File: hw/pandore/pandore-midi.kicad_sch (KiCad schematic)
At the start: 0 parts

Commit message: added all remaining connectors (only missing M.2 now)
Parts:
- added J10: MIDI_in, reekilib_con:samesky_SDS-50J, symbol reekilib_con:MIDI_in
- added J11: MIDI_out, reekilib_con:samesky_SDS-50J, symbol reekilib_con:MIDI_out

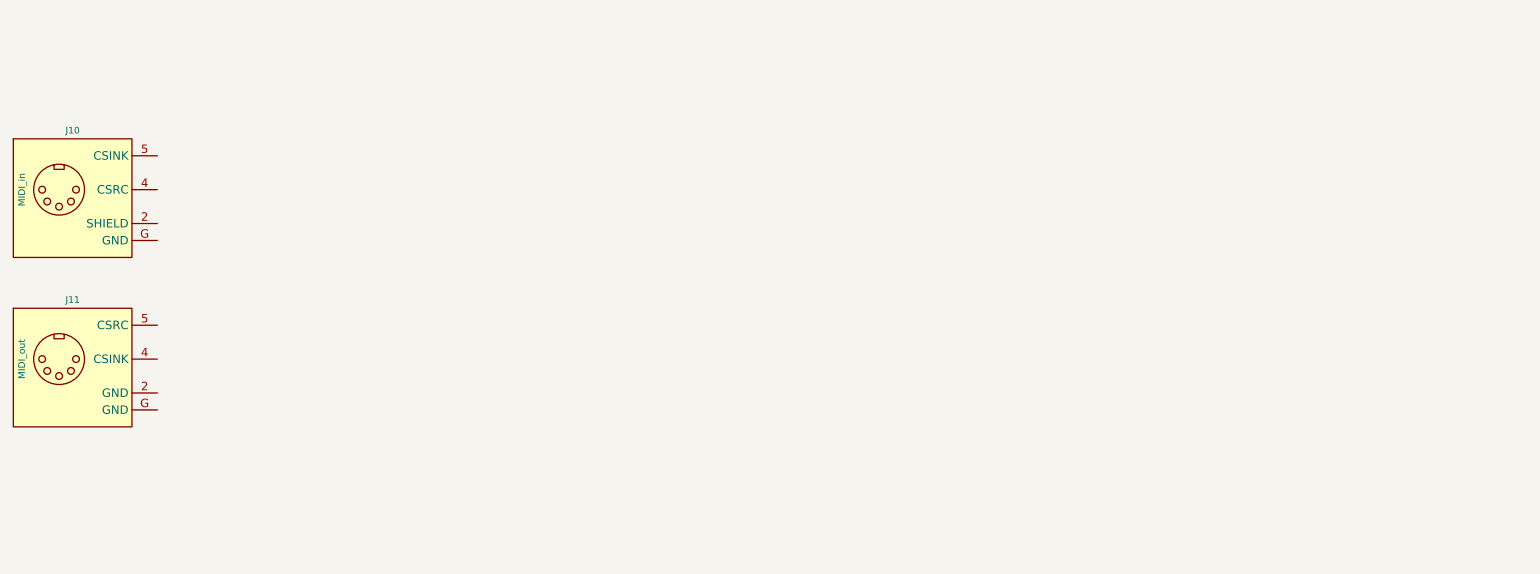
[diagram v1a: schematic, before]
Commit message: Added lots to sch and pcb: eth passive, audio codec, midi, teensy Corrected and added support for M.2
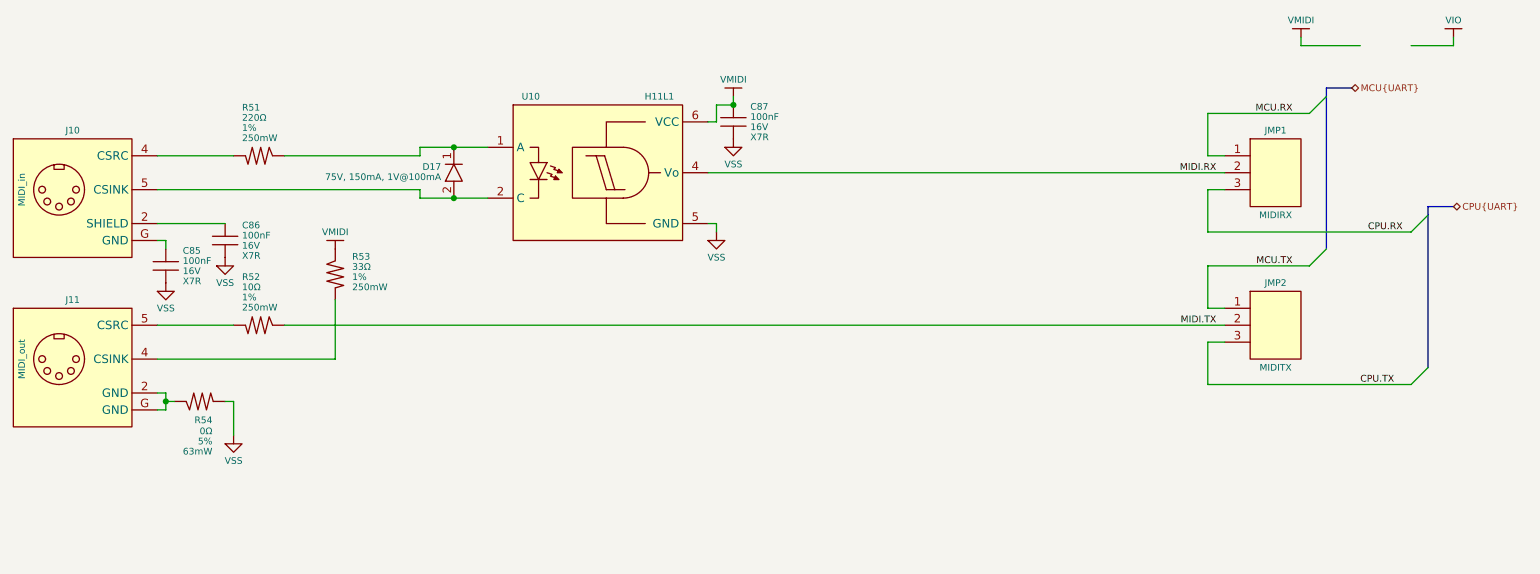
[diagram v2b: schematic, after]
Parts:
- added C85, C86, C87: ${Capacitance}, ${Voltage}, ${Dielectric}, reekilib_cap:CAPC1005, symbol reekilib_cap:cap
- added D17: ${Vr}, ${Io}, ${Vf}, reekilib_sod:sod-123, symbol reekilib_dio:diode
- added JMP1: MIDIRX, reekilib_con:HDR254P1X03-TH, symbol reekilib_con:hdr-1x3
- added JMP2: MIDITX, reekilib_con:HDR254P1X03-TH, symbol reekilib_con:hdr-1x3
- added R51, R52, R53: ${Resistance}, ${Tolerance}, ${Power}, reekilib_res:RESC2012, symbol reekilib_res:res
- added R54: ${Resistance}, ${Tolerance}, ${Power}, reekilib_res:RESC1005, symbol reekilib_res:res
- added U10: H11L1, reekilib_soic:SOIC254P1030X430-6, symbol reekilib_iso:opto_digppout
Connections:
- net at J10.2 (SHIELD): now also C86.2
- net at J10.4 (CSRC): now also R51.1
- net at J10.5 (CSINK): now also D17.2 (A), U10.2 (C)
- net at J10.G (GND): now also C85.2
- net at J11.2 (GND): now also J11.G (GND), R54.2
- net at J11.4 (CSINK): now also R53.1
- net at J11.5 (CSRC): now also R52.1
- new net: D17.1 (C), R51.2, U10.1 (A)
- new net CPU.RX: JMP1.3
- new net CPU.TX: JMP2.3
- new net MCU.RX: JMP1.1
- new net MCU.TX: JMP2.1
- new net MIDI.RX: JMP1.2, U10.4 (Vo)
- new net MIDI.TX: JMP2.2, R52.2
- new net VMIDI: C87.2, R53.2, U10.6 (VCC)
- new net VSS: C85.1, C86.1, C87.1, R54.1, U10.5 (GND)

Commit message: most of board control signals added, routed and defined
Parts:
- C85, C86: footprint reekilib_cap:CAPC1005 -> reekilib_cap:CAPC3216; Capacitance 100nF -> 100pF; Dielectric X7R -> X5R; Link https://www.passivecomponent.com/product-search/MLCC/?partn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 -> (none); MFG Walsin Technology Corporation -> (none); MFG2 Samsung Electro-Mechanics -> (none); MFG3 Taiyo Yuden -> (none); MFG4 YAGEO -> (none); MPN 0402B104K160CT -> (none); MPN2 CL05B104KA5NNNC -> (none); MPN3 EMK105B7104KV-F -> (none); MPN4 CC0402KRX7R7BB104 -> (none); Voltage 16V -> 1kV
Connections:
- net VSS: now also C85.2, C86.2; no longer C85.1, C86.1
- net at J10.2 (SHIELD): now also C86.1; no longer C86.2
- net at J10.G (GND): now also C85.1; no longer C85.2

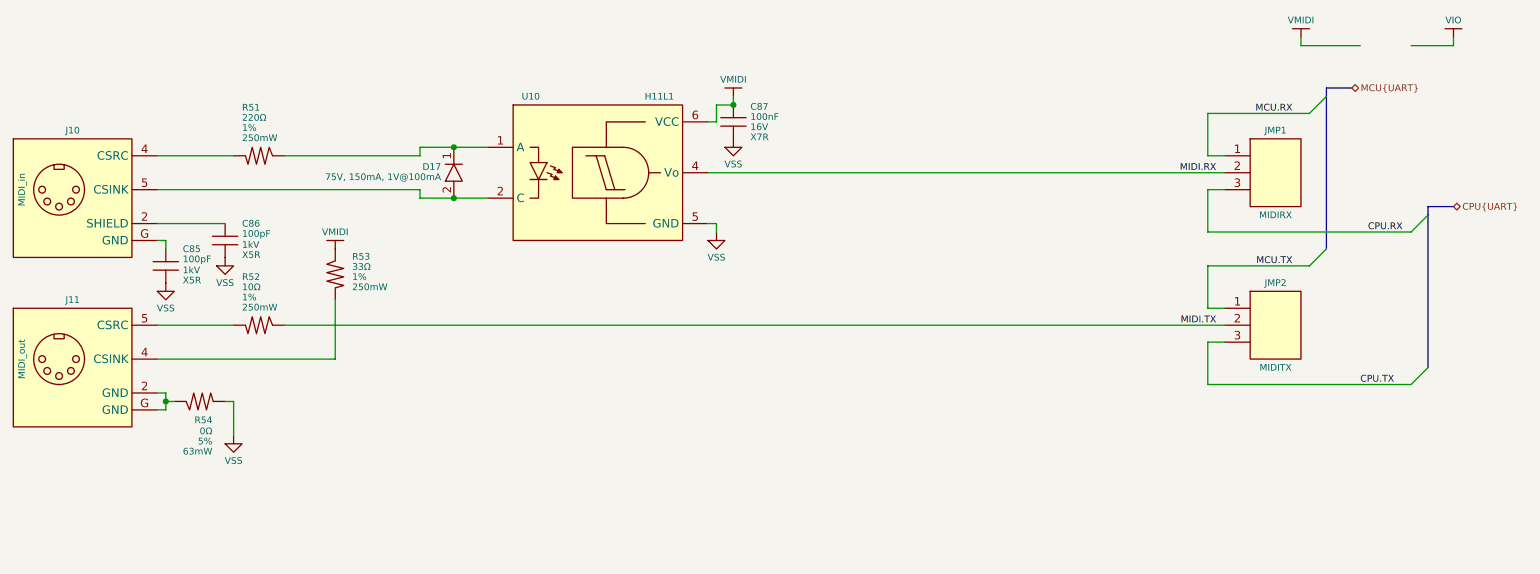
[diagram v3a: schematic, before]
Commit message: more routing/placement done added 5v load switch 1A each added second fan circuit redone all diffpair routing following new stackup calc added all (?) missing connectors to unused pins
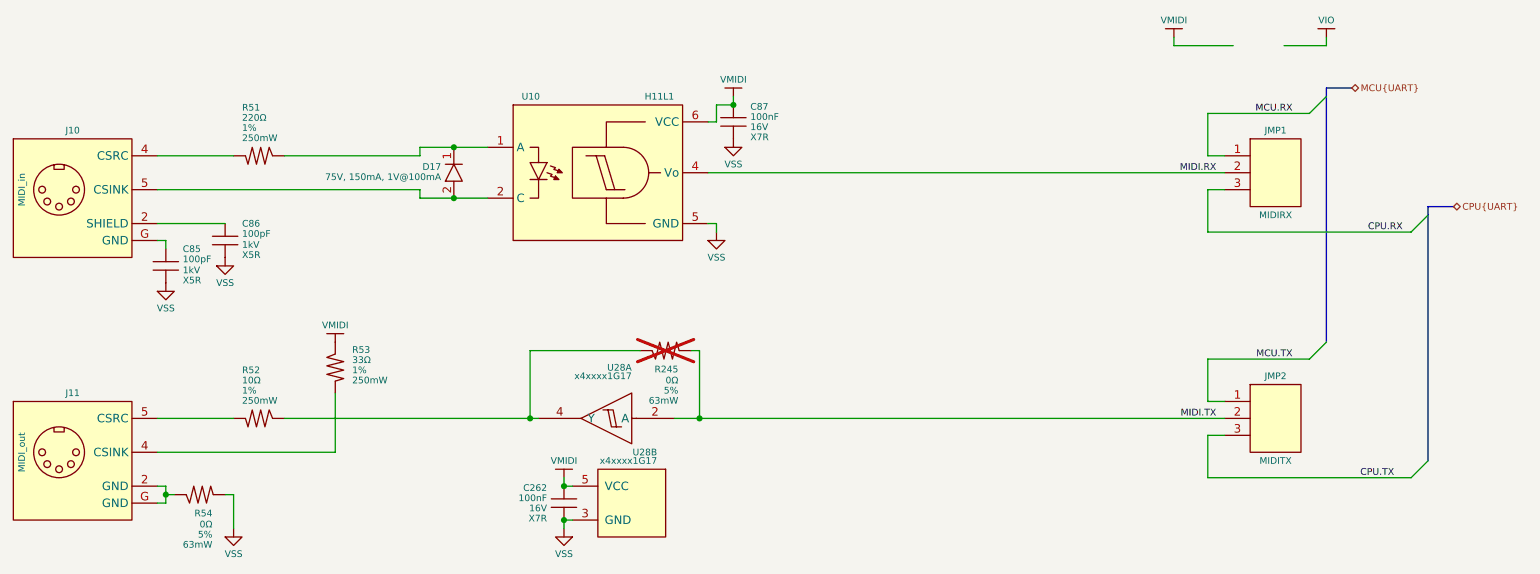
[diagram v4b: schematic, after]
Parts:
- added C262: ${Capacitance}, ${Voltage}, ${Dielectric}, reekilib_cap:CAPC1005, symbol reekilib_cap:cap
- added R245: ${Resistance}, ${Tolerance}, ${Power}, reekilib_res:RESC1005, symbol reekilib_res:res
- added U28: x4xxxx1G17, reekilib_sot:SOT65P210X90-5, symbol reekilib_log:x4xxxx1G17
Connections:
- net MIDI.TX: now also R245.1, U28.2 (A); no longer R52.2
- net VMIDI: now also C262.2, U28.5 (VCC)
- net VSS: now also C262.1, U28.3 (GND)
- new net: R245.2, R52.2, U28.4 (Y)
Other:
- moved on the sheet: J11, JMP2, R52, R53, R54

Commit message: finished adding mpn,mfg to all parts, finished routing placement
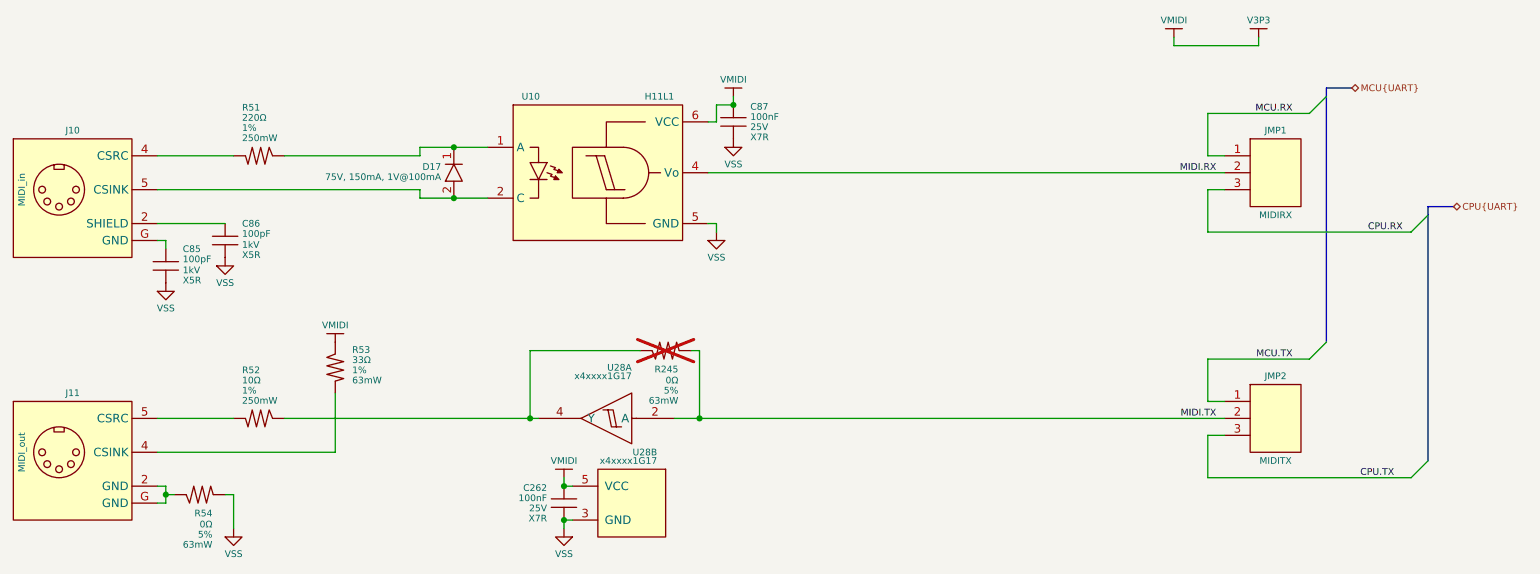
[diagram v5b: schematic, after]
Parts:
- C262, C87: MFG2 Samsung Electro-Mechanics -> (none); MFG3 Taiyo Yuden -> (none); MPN2 CL05B104KA5NNNC -> (none); MPN3 EMK105B7104KV-F -> (none); Voltage 16V -> 25V
- C85, C86: MFG (none) -> Vishay Vitramon; MPN (none) -> VJ1206A101JXGCW1HV
- JMP1, JMP2: Link url-link -> (none); MFG MFG -> Adam Tech; MPN MPN -> PH1-03-UA
- R245, R54: Link (none) -> https://yageogroup.com/products/Resistors/part/RC0402JR-070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; MFG (none) -> Yageo; MFG2 (none) -> Stackpole; MFG3 (none) -> Vishay Dale; MPN (none) -> RC0402JR-070RL; MPN2 (none) -> RMCF0402ZT0R00; MPN3 (none) -> CRCW04020000Z0ED
- R51: MFG (none) -> Susumu; MPN (none) -> RR1220P-221-D
- R52: value ${Resistance}, ${Tolerance}, ${Power} -> ${Resistance}, ${Tolerance}, ${Type}; MFG (none) -> Stackpole Electronics Inc; MPN (none) -> RNCF0805DTE10R0
- R53: footprint reekilib_res:RESC2012 -> reekilib_res:RESC1005; Link (none) -> https://yageogroup.com/products/Resistors/part/RC0402FR-073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; MFG (none) -> YAGEO; MPN (none) -> RC0402FR-0733RL; Power 250mW -> 63mW
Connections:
- net VMIDI renamed V3P3

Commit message: DRC passing
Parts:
- R52: Type (none) -> thin film
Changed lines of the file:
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@@
 				)
 				(justify right)
+				(hide yes)
 			)
 		)
@@
 				(justify left)
 				(hide yes)
+			)
+		)
+		(property "Type" "thin film"
+			(at 78.74 76.2 90)
+			(effects
+				(font
+					(size 1.016 1.016)
+				)
+				(justify right)
 			)
 		)
@@
 		(on_board no)
 		(dnp no)
-		(property "Reference" "#PWR?"
+		(property "Reference" "#PWR0393"
 			(at 231.14 17.145 0)
 			(do_not_autoplace yes)
@@
 			(project "pandore"
 				(path "/e55f2700-f75a-4062-8a27-fe258faa8966/22b3123e-4770-49db-9ca3-fb0ae5205bb3"
-					(reference "#PWR?")
+					(reference "#PWR0393")
 					(unit 1)
 				)
@@
 		(pin "4"
 		)
+		(pin "3"
+		)
 		(instances
